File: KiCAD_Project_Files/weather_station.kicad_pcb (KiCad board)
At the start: 2 copper layers, 90 x 32 mm, 59 parts, among them J1 JST-XH, J2 SMA Antenna Connector, J3 Debug Connector, M1 Mounting_Wuerth_WA-SMSI-M1.6_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, M2 Mounting_Wuerth_WA-SMSI-M1.6_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, SW1 SW_MAIN_PWR, U1 RFM95W-868S2R, U10 TPS61023DRLR, U2 MICS-6814, U3 STM32F301C8T6TR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

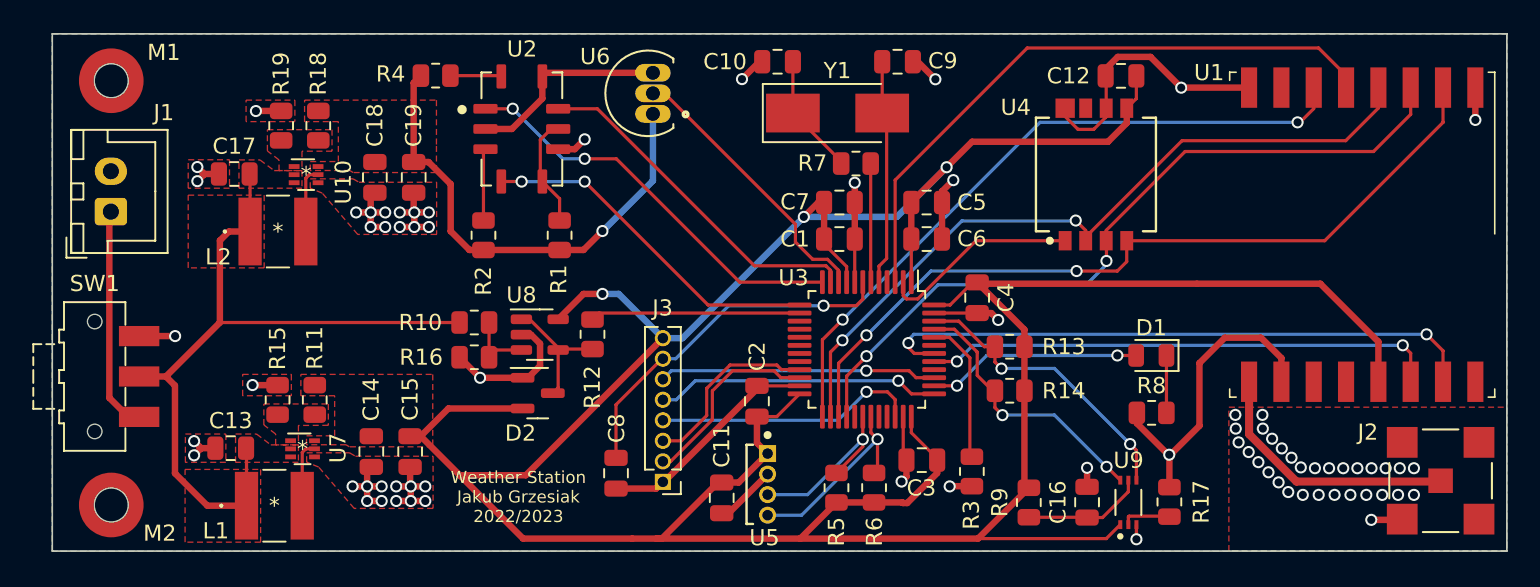
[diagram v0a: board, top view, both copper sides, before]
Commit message: Updated PCB and added 3D view
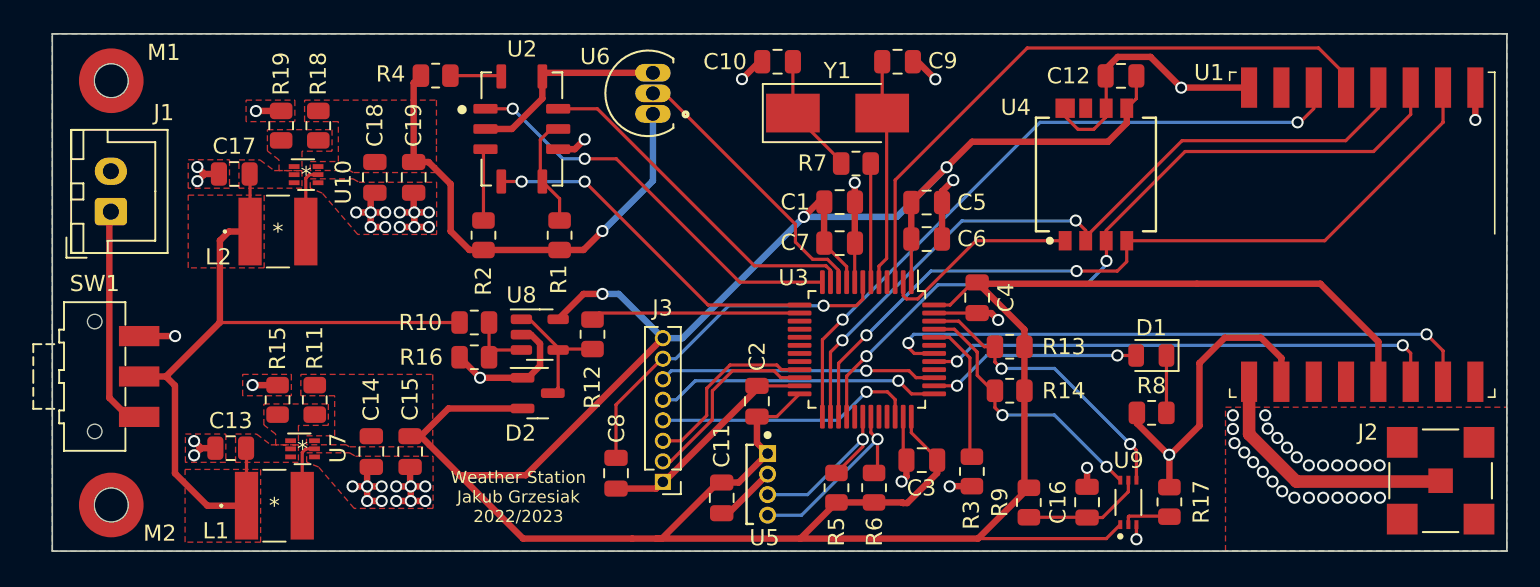
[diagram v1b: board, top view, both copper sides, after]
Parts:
- J3: value Debug Connector -> Programming/Debug Connector
- moved C7 2.51 mm to (115.3, 66.5)
- moved C1 2.29 mm to (115.3, 64.0)
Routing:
- net GND: track 137.1 -> 135.1 mm, vias 74 -> 69
